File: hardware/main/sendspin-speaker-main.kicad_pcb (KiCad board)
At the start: 2 copper layers, 0 parts

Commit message: hardware: footprints and nets in all three boards, JLC design rules
- Update PCB from Schematic on main, front panel and USB-C board.
- Design rules for JLCPCB 2-layer (0.15 mm track/clearance, 0.3 mm
  drill, 0.6 mm vias, 0.3 mm to the edge); net classes Power (1.0 mm),
  Speaker (0.6 mm), Supply3V3 (0.4 mm).
- TP4056 on the SOIC-8-EP footprint without 0.2 mm thermal vias;
  MSK12C02 footprint marked SMD, its shell pads to GND.
- Generator keeps symbol UUIDs stable so regenerated sheets stay linked.

Co-Authored-By: Claude Opus 5.5 <noreply@anthropic.com>
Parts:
- added C101: 22u, Capacitor_SMD:C_0805_2012Metric, F.Cu at (171.7, 113.8)
- added C102: 100n, Capacitor_SMD:C_0805_2012Metric, F.Cu at (171.7, 116.8)
- added C103: 1u, Capacitor_SMD:C_0805_2012Metric, F.Cu at (171.7, 119.8)
- added C201: 10u, Capacitor_SMD:C_0805_2012Metric, F.Cu at (182.6, 118.1)
- added C202: 10u, Capacitor_SMD:C_0805_2012Metric, F.Cu at (182.6, 121.1)
- added C203: 100n, Capacitor_SMD:C_0805_2012Metric, F.Cu at (182.6, 124.1)
- added C204: 10u, Capacitor_SMD:C_0805_2012Metric, F.Cu at (182.6, 127.1)
- added C205: 10u, Capacitor_SMD:C_0805_2012Metric, F.Cu at (182.6, 130.1)
- added C206: 10u, Capacitor_SMD:C_0805_2012Metric, F.Cu at (182.6, 133.2)
- added C207: 100n, Capacitor_SMD:C_0805_2012Metric, F.Cu at (182.6, 136.2)
- added C301: 1u, Capacitor_SMD:C_0805_2012Metric, F.Cu at (182.6, 160.3)
- added C302: 1u, Capacitor_SMD:C_0805_2012Metric, F.Cu at (182.6, 163.3)
- added C303: 100n, Capacitor_SMD:C_0805_2012Metric, F.Cu at (182.6, 166.4)
- added C401: 100n, Capacitor_SMD:C_0805_2012Metric, F.Cu at (144.2, 150.4)
- added C402: 100n, Capacitor_SMD:C_0805_2012Metric, F.Cu at (144.2, 153.4)
- added C403: 1u, Capacitor_SMD:C_0805_2012Metric, F.Cu at (144.2, 156.4)
- added C404: 10u, Capacitor_SMD:C_0805_2012Metric, F.Cu at (144.2, 159.4)
- added C405: 1u, Capacitor_SMD:C_0805_2012Metric, F.Cu at (148.7, 150.4)
- added C411: 100n, Capacitor_SMD:C_0805_2012Metric, F.Cu at (148.7, 153.4)
- added C412: 100n, Capacitor_SMD:C_0805_2012Metric, F.Cu at (148.7, 156.4)
- added C413: 1u, Capacitor_SMD:C_0805_2012Metric, F.Cu at (148.7, 159.4)
- added C414: 10u, Capacitor_SMD:C_0805_2012Metric, F.Cu at (153.1, 150.4)
- added C415: 1u, Capacitor_SMD:C_0805_2012Metric, F.Cu at (153.1, 153.4)
- added C421: 470u, Capacitor_SMD:CP_Elec_8x10, F.Cu at (163.5, 142.8)
- added C422: 47u, Capacitor_SMD:C_0805_2012Metric, F.Cu at (153.1, 156.4)
- added C423: 47u, Capacitor_SMD:C_0805_2012Metric, F.Cu at (153.1, 159.4)
- added D101: green, LED_SMD:LED_0805_2012Metric, F.Cu at (171.7, 122.8)
- added D201: red, LED_SMD:LED_0805_2012Metric, F.Cu at (204.1, 137.6)
- added D202: green, LED_SMD:LED_0805_2012Metric, F.Cu at (204.1, 140.6)
- added D203: BAT54W, Package_TO_SOT_SMD:SOT-323_SC-70, F.Cu at (199.9, 137.8)
- added D204: BAT54W, Package_TO_SOT_SMD:SOT-323_SC-70, F.Cu at (199.9, 141.1)
- added D205: SS34, Diode_SMD:D_SMA, F.Cu at (202.0, 133.8)
- added J201: J_BAT, Connector_JST:JST_PH_B2B-PH-K_1x02_P2.00mm_Vertical, F.Cu at (187.8, 134.2)
- added J202: J_SW, Connector_JST:JST_XH_B2B-XH-A_1x02_P2.50mm_Vertical, F.Cu at (200.2, 120.0)
- added J203: J_CHG, Connector_JST:JST_XH_B3B-XH-A_1x03_P2.50mm_Vertical, F.Cu at (188.3, 120.0)
- added J301: J_USB, Connector_JST:JST_XH_B4B-XH-A_1x04_P2.50mm_Vertical, F.Cu at (188.3, 162.2)
- added J401: J_SPK_L, Connector_JST:JST_XH_B2B-XH-A_1x02_P2.50mm_Vertical, F.Cu at (158.8, 152.3)
- added J402: J_SPK_R, Connector_JST:JST_XH_B2B-XH-A_1x02_P2.50mm_Vertical, F.Cu at (158.8, 160.1)
- added J403: PJ-320D, lcsc:AUDIO-SMD_PJ-320D-1, F.Cu at (152.0, 143.4)
- added J501: J_UI, Connector_JST:JST_XH_B12B-XH-A_1x12_P2.50mm_Vertical, F.Cu at (179.4, 102.4)
- added J502: J_LED, Connector_JST:JST_XH_B3B-XH-A_1x03_P2.50mm_Vertical, F.Cu at (179.4, 110.2)
- added JP201: SW bypass, Jumper:SolderJumper-2_P1.3mm_Open_RoundedPad1.0x1.5mm, F.Cu at (182.5, 139.4)
- added Q201: FS8205A, lcsc:SOT-23-6_L2.9-W1.6-P0.95-LS2.8-BR, F.Cu at (187.2, 140.2)
- added Q202: AO3401A, Package_TO_SOT_SMD:SOT-23, F.Cu at (195.2, 143.0)
- added Q301: UMH3N, Package_TO_SOT_SMD:SOT-363_SC-70-6, F.Cu at (197.1, 168.5)
- added R101: 10k, Resistor_SMD:R_0805_2012Metric, F.Cu at (167.3, 113.8)
- added R102: 10k, Resistor_SMD:R_0805_2012Metric, F.Cu at (167.3, 116.7)
- added R103: 10k, Resistor_SMD:R_0805_2012Metric, F.Cu at (167.3, 119.7)
- added R104: 10k, Resistor_SMD:R_0805_2012Metric, F.Cu at (167.3, 122.6)
- added R105: 4.7k, Resistor_SMD:R_0805_2012Metric, F.Cu at (167.3, 125.6)
- added R106: 4.7k, Resistor_SMD:R_0805_2012Metric, F.Cu at (167.3, 128.5)
- added R107: 10k, Resistor_SMD:R_0805_2012Metric, F.Cu at (167.3, 131.5)
- added R108: 1k, Resistor_SMD:R_0805_2012Metric, F.Cu at (167.3, 134.4)
- added R201: 2.4k, Resistor_SMD:R_0805_2012Metric, F.Cu at (178.1, 118.1)
- added R202: 1k, Resistor_SMD:R_0805_2012Metric, F.Cu at (178.1, 121.0)
- added R203: 1k, Resistor_SMD:R_0805_2012Metric, F.Cu at (178.1, 124.0)
- added R204: 100, Resistor_SMD:R_0805_2012Metric, F.Cu at (178.1, 126.9)
- added R205: 1k, Resistor_SMD:R_0805_2012Metric, F.Cu at (178.1, 129.9)
- added R206: 100k, Resistor_SMD:R_0805_2012Metric, F.Cu at (178.1, 132.8)
- added R207: 470k, Resistor_SMD:R_0805_2012Metric, F.Cu at (178.1, 135.8)
- added R208: 470k, Resistor_SMD:R_0805_2012Metric, F.Cu at (178.1, 138.7)
- added R301: 5.1k, Resistor_SMD:R_0805_2012Metric, F.Cu at (178.1, 148.7)
- added R302: 5.1k, Resistor_SMD:R_0805_2012Metric, F.Cu at (178.1, 151.6)
- added R303: 470, Resistor_SMD:R_0805_2012Metric, F.Cu at (178.1, 154.6)
- added R304: 470, Resistor_SMD:R_0805_2012Metric, F.Cu at (178.1, 157.5)
- added R401: 100k, Resistor_SMD:R_0805_2012Metric, F.Cu at (167.0, 150.4)
- added R402: 100k, Resistor_SMD:R_0805_2012Metric, F.Cu at (167.0, 153.3)
- added R411: 100k, Resistor_SMD:R_0805_2012Metric, F.Cu at (167.0, 156.3)
- added R412: 100k, Resistor_SMD:R_0805_2012Metric, F.Cu at (167.0, 159.2)
- added R421: 100k, Resistor_SMD:R_0805_2012Metric, F.Cu at (167.0, 162.2)
- added R501: 330, Resistor_SMD:R_0805_2012Metric, F.Cu at (190.1, 108.3)
- added SW101: Reset, Button_Switch_SMD:SW_Push_1P1T_XKB_TS-1187A, F.Cu at (169.4, 102.3)
- added SW102: Boot, Button_Switch_SMD:SW_Push_1P1T_XKB_TS-1187A, F.Cu at (169.4, 109.0)
- added SW201: MSK12C02, lcsc:SW-TH_MSK12C02, F.Cu at (189.5, 127.4)
- added U101: ESP32-A1S, lcsc:WIRELM-SMD_ESP32-A1S, F.Cu at (153.6, 118.7)
- added U201: TP4056, Package_SO:SOIC-8-1EP_3.9x4.9mm_P1.27mm_EP2.41x3.3mm, F.Cu at (198.4, 127.8)
- added U202: DW01A, Package_TO_SOT_SMD:SOT-23-6, F.Cu at (195.3, 133.9)
- added U203: AP2112K-3.3, Package_TO_SOT_SMD:SOT-23-5, F.Cu at (195.3, 138.5)
- added U301: USBLC6-2SC6, Package_TO_SOT_SMD:SOT-23-6, F.Cu at (187.4, 169.0)
- added U302: CH340C, Package_SO:SOIC-16_3.9x9.9mm_P1.27mm, F.Cu at (184.6, 153.1)
- added U303: XC6206P332MR, Package_TO_SOT_SMD:SOT-23-3, F.Cu at (192.5, 168.9)
- added U401: NS4150B, lcsc:MSOP-8_L3.0-W3.0-P0.65-LS5.0-BL, F.Cu at (144.4, 164.4)
- added U402: NS4150B, lcsc:MSOP-8_L3.0-W3.0-P0.65-LS5.0-BL, F.Cu at (149.1, 164.4)
- added USB301: USB-C, Connector_USB:USB_C_Receptacle_HRO_TYPE-C-31-M-12, F.Cu at (194.6, 153.0)

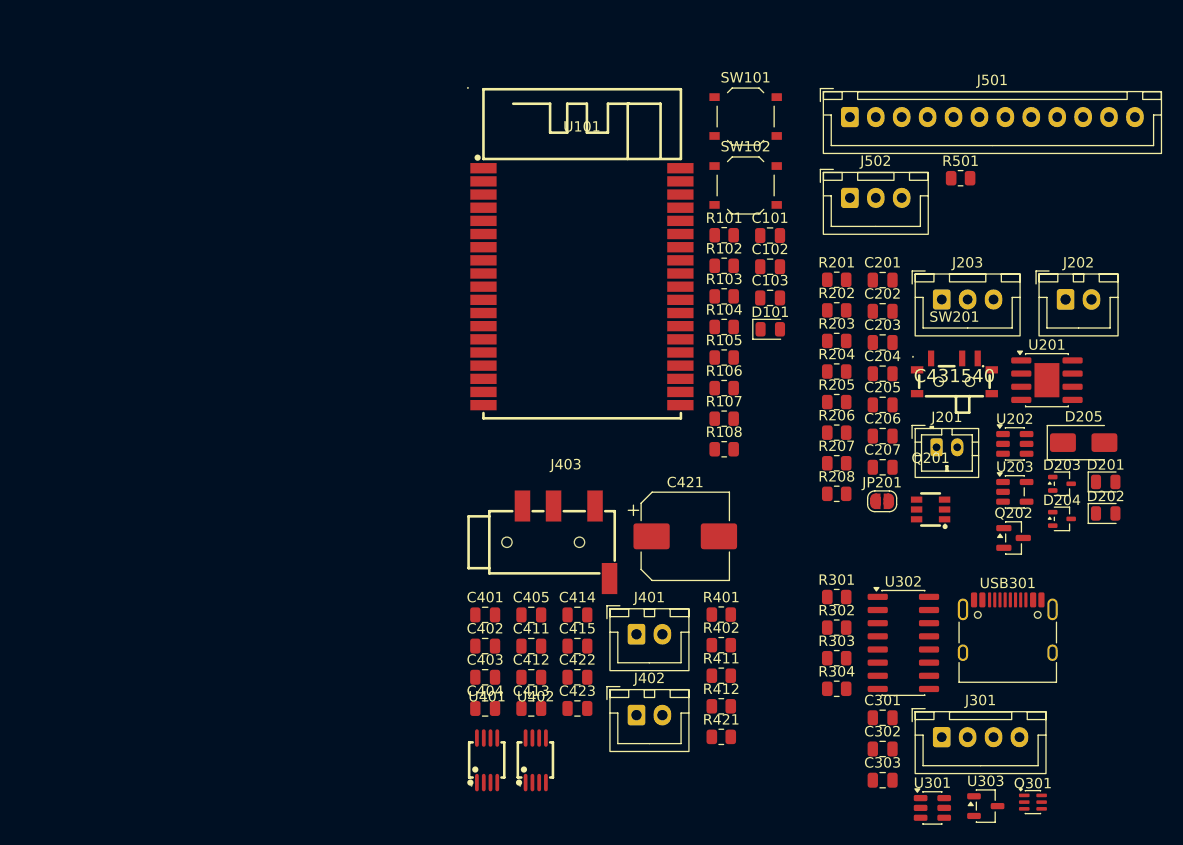
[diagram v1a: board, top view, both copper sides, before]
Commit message: hardware: first placement of all three boards
Outlines, mounting holes, edge connectors, parts by function and GND
pours, written with KiCad's Python (scripts/pcbplace.py, place_*.py).
DRC: no copper or courtyard errors; unrouted connections and silkscreen
text remain. Renders in hardware/docs/.

Co-Authored-By: Claude Opus 5.5 <noreply@anthropic.com>
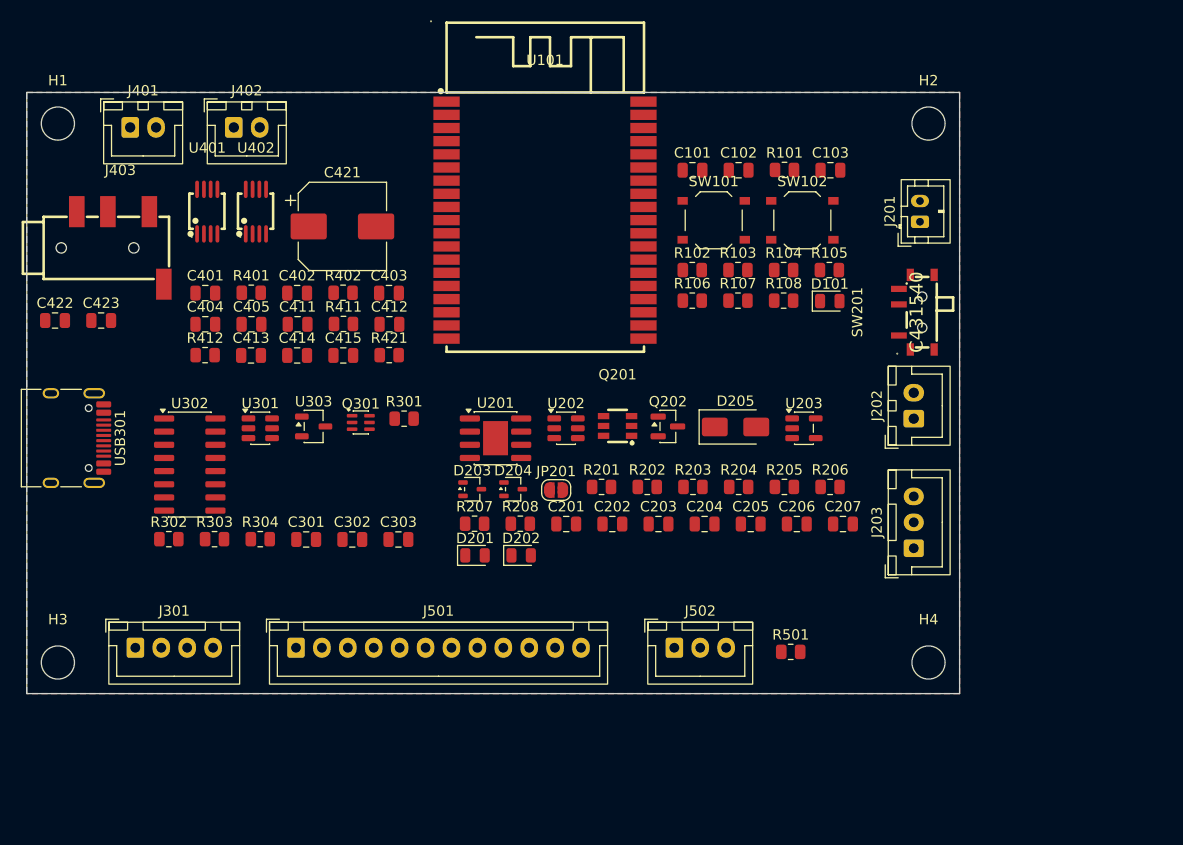
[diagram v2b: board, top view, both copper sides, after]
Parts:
- added H1: MountingHole_3.2mm_M3, MountingHole:MountingHole_3.2mm_M3, F.Cu at (103.0, 103.0)
- added H2: MountingHole_3.2mm_M3, MountingHole:MountingHole_3.2mm_M3, F.Cu at (187.0, 103.0)
- added H3: MountingHole_3.2mm_M3, MountingHole:MountingHole_3.2mm_M3, F.Cu at (103.0, 155.0)
- added H4: MountingHole_3.2mm_M3, MountingHole:MountingHole_3.2mm_M3, F.Cu at (187.0, 155.0)
- moved USB301 93.4 mm to (103.4, 133.3), turned to -90 degrees
- moved J301 78.3 mm to (110.5, 153.6)
- moved U303 74.5 mm to (127.7, 132.2)
- moved Q301 74.5 mm to (132.2, 131.8)
- moved U301 74.5 mm to (122.5, 132.4)
- moved J501 74.0 mm to (126.0, 153.6)
- moved U302 71.0 mm to (115.7, 135.9)
- moved J401 69.1 mm to (110.0, 103.4)
- moved J402 68.7 mm to (120.0, 103.4)
- moved R302 65.0 mm to (113.7, 143.1)
- moved D201 61.3 mm to (143.2, 144.7)
- moved R303 61.1 mm to (118.1, 143.1)
- moved C422 61.0 mm to (102.7, 122.0)
- moved R412 60.2 mm to (117.2, 125.3)
- moved U401 59.4 mm to (117.4, 111.5)
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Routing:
- added copper zone on B.Cu, net GND
- added copper zone on F.Cu, net GND
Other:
- board outline added: 90 x 58 mm

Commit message: hardware: bare panel/USB-C boards updated, XH battery, holes in, round corners
- Boards updated from the schematics: J_USB XH 6 with CC1/CC2, panel
  without parts (J604 LED header), USB-C board without parts.
- J_BAT JST XH 2.
- M3 holes 4.5 mm in from the edges (heads stay on the board), M2 3 mm;
  rounded corners. DRC: no copper, courtyard or outline errors.

Co-Authored-By: Claude Opus 5.5 <noreply@anthropic.com>
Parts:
- J201: footprint Connector_JST:JST_PH_B2B-PH-K_1x02_P2.00mm_Vertical -> Connector_JST:JST_XH_B2B-XH-A_1x02_P2.50mm_Vertical
- J301: footprint Connector_JST:JST_XH_B4B-XH-A_1x04_P2.50mm_Vertical -> Connector_JST:JST_XH_B6B-XH-A_1x06_P2.50mm_Vertical
- moved J501 6.50 mm to (132.5, 153.6)
- moved J502 5.00 mm to (167.5, 153.6)
- moved R501 4.50 mm to (178.2, 154.0)
- moved J201 2.57 mm to (185.6, 115.0)
- moved J401 2.50 mm to (112.5, 103.4)
- moved J402 2.50 mm to (122.5, 103.4)
- moved H1 2.12 mm to (104.5, 104.5)
- moved H2 2.12 mm to (185.5, 104.5)
- moved H3 2.12 mm to (104.5, 153.5)
- moved H4 2.12 mm to (185.5, 153.5)
- moved J301 2.00 mm to (112.5, 153.6)
- moved SW201 2.00 mm to (185.8, 123.2)
- moved J202 1.50 mm to (185.6, 133.0)
- moved J203 1.00 mm to (185.6, 145.0)
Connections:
- J301 pad 4: GND -> /USB/CC1
- J501 pad 12: /LED -> /Connectors/LED_EXT
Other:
- outline, holes or cut-outs redrawn

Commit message: hardware: main board passives at their pins, amps by the speaker outputs
place_main.py puts each passive next to the pin it serves (nearest free
spot, pcbplace.near); amps and speaker connectors move to the right of
the module. Connection length 2472 -> 1906 mm. PJ-320D footprint: added
courtyard, 3D model offset onto its pads. DRC: no copper/courtyard errors.

Co-Authored-By: Claude Opus 5.5 <noreply@anthropic.com>
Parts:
- moved SW102 62.1 mm to (113.3, 103.8)
- moved C404 54.8 mm to (170.9, 111.3)
- moved J401 52.0 mm to (164.5, 103.4)
- moved C207 51.6 mm to (136.5, 112.0)
- moved J402 51.5 mm to (174.0, 103.4)
- moved U401 51.3 mm to (168.6, 115.9)
- moved D101 49.6 mm to (128.5, 112.3)
- moved U402 48.2 mm to (168.6, 124.4)
- moved C421 46.9 mm to (176.6, 121.0)
- moved C401 46.8 mm to (163.9, 115.6)
- moved C405 46.6 mm to (166.9, 111.3)
- moved C414 46.3 mm to (172.4, 126.8)
- moved R108 45.7 mm to (128.5, 109.8)
- moved R105 45.4 mm to (132.5, 110.5)
- moved SW101 43.8 mm to (123.3, 103.8)
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
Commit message: hardware: main board routed and labelled, JLC files
- Freerouting (jar, portable Java 25) via scripts/route.py; net classes
  Power 0.8 mm / Supply 0.4 mm so tracks fit the fine-pitch pins.
- Silkscreen pin names and function labels (silk_main.py), references on
  the fab layer, SMD GND pads solid to the pour; board 100 x 58 mm.
- LCSC numbers on all SMD parts (checked on lcsc.com); jlc.py writes the
  Gerber ZIP, BOM and CPL in JLC's formats.

Co-Authored-By: Claude Opus 5.5 <noreply@anthropic.com>
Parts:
- moved R207 31.6 mm to (154.5, 135.5)
- moved R421 16.2 mm to (160.6, 129.1)
- moved Q201 14.7 mm to (164.5, 116.9)
- moved C405 14.1 mm to (180.4, 115.2)
- moved C103 12.2 mm to (163.5, 120.2)
- moved H2 10.0 mm to (195.5, 104.5)
- moved H4 10.0 mm to (195.5, 153.5)
- moved J201 10.0 mm to (195.6, 115.0)
- moved J202 10.0 mm to (195.6, 133.0)
- moved J203 10.0 mm to (195.6, 145.0)
- moved SW201 10.0 mm to (195.8, 123.2)
- moved C401 9.50 mm to (163.9, 125.0)
- moved C205 8.60 mm to (156.4, 141.1)
- moved D202 8.38 mm to (137.5, 142.7)
- moved R402 7.07 mm to (156.0, 126.5)
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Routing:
- net GND: track 0.00 -> 503.4 mm, vias 0 -> 7
- net /VBUS: track 0.00 -> 175.2 mm, vias 0 -> 7
- net /EN: track 0.00 -> 150.3 mm, vias 0 -> 4
- net +3V3: track 0.00 -> 145.5 mm, vias 0 -> 7
- net VBAT_SW: track 0.00 -> 135.0 mm, vias 0 -> 2
- net /IO0: track 0.00 -> 85.3 mm, vias 0 -> 3
- net /U0RXD: track 0.00 -> 76.2 mm, vias 0 -> 2
- net /LED: track 0.00 -> 74.9 mm, vias 0 -> 4
- net VBAT: track 0.00 -> 73.7 mm, vias 0 -> 3
- net /Power/VBAT_LS: track 0.00 -> 69.7 mm, vias 0 -> 3
- net /U0TXD: track 0.00 -> 65.0 mm, vias 0 -> 2
- net /HPOUTR: track 0.00 -> 64.4 mm, vias 0 -> 2
- net /VBAT_SENSE: track 0.00 -> 64.0 mm, vias 0 -> 3
- net /Power/CHRG_K: track 0.00 -> 63.9 mm, vias 0 -> 2
- net /Power/STDBY_K: track 0.00 -> 62.4 mm
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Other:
- board size 90 x 58 mm -> 100 x 58 mm
- board text added: "+"
- board text added: "-"
- board text added: "3V3"
- board text added: "5V"
- board text added: "B1"
- board text added: "B3"
- board text added: "B4"
- board text added: "B5"
- board text added: "B6"
- board text added: "BAT"
- board text added: "BOOT"
- board text added: "BYPASS"
- board text added: "CC1"
- board text added: "CC2"
- board text added: "CERN-OHL-P-2.0 github.com/Boisti13/esp32-sendspin-speaker"
- board text added: "CHARGE"
- board text added: "CHG"
- board text added: "CS"
- board text added: "D+"
- board text added: "D-"
- board text added: "DC"
- board text added: "ESP32 Sendspin Speaker"
- board text added: "FULL"
- board text added: "GND"
- board text added: "LED"
- board text added: "MOSI"
- board text added: "ON/OFF"
- board text added: "PANEL"
- board text added: "PHONES"
- board text added: "RESET"
- board text added: "SCK"
- board text added: "SPK L"
- board text added: "SPK R"
- board text added: "STATUS"
- board text added: "SW"
- board text added: "SWITCH"
- board text added: "USB"
- board text added: "USB-C"
- board text added: "V+"
- board text added: "main board Rev A 2026-10"
